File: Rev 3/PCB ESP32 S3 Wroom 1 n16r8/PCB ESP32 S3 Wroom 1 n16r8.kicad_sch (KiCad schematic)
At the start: 30 parts, among them J1 AudioJack3_SwitchT, M1 Haptic Feedback, Q1 BS170, SW1 Home, SW2 Back, SW3 Play/Pause, SW4 Power, SW5 Menu, SW6 Hold, SW7 BOOT_MODE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

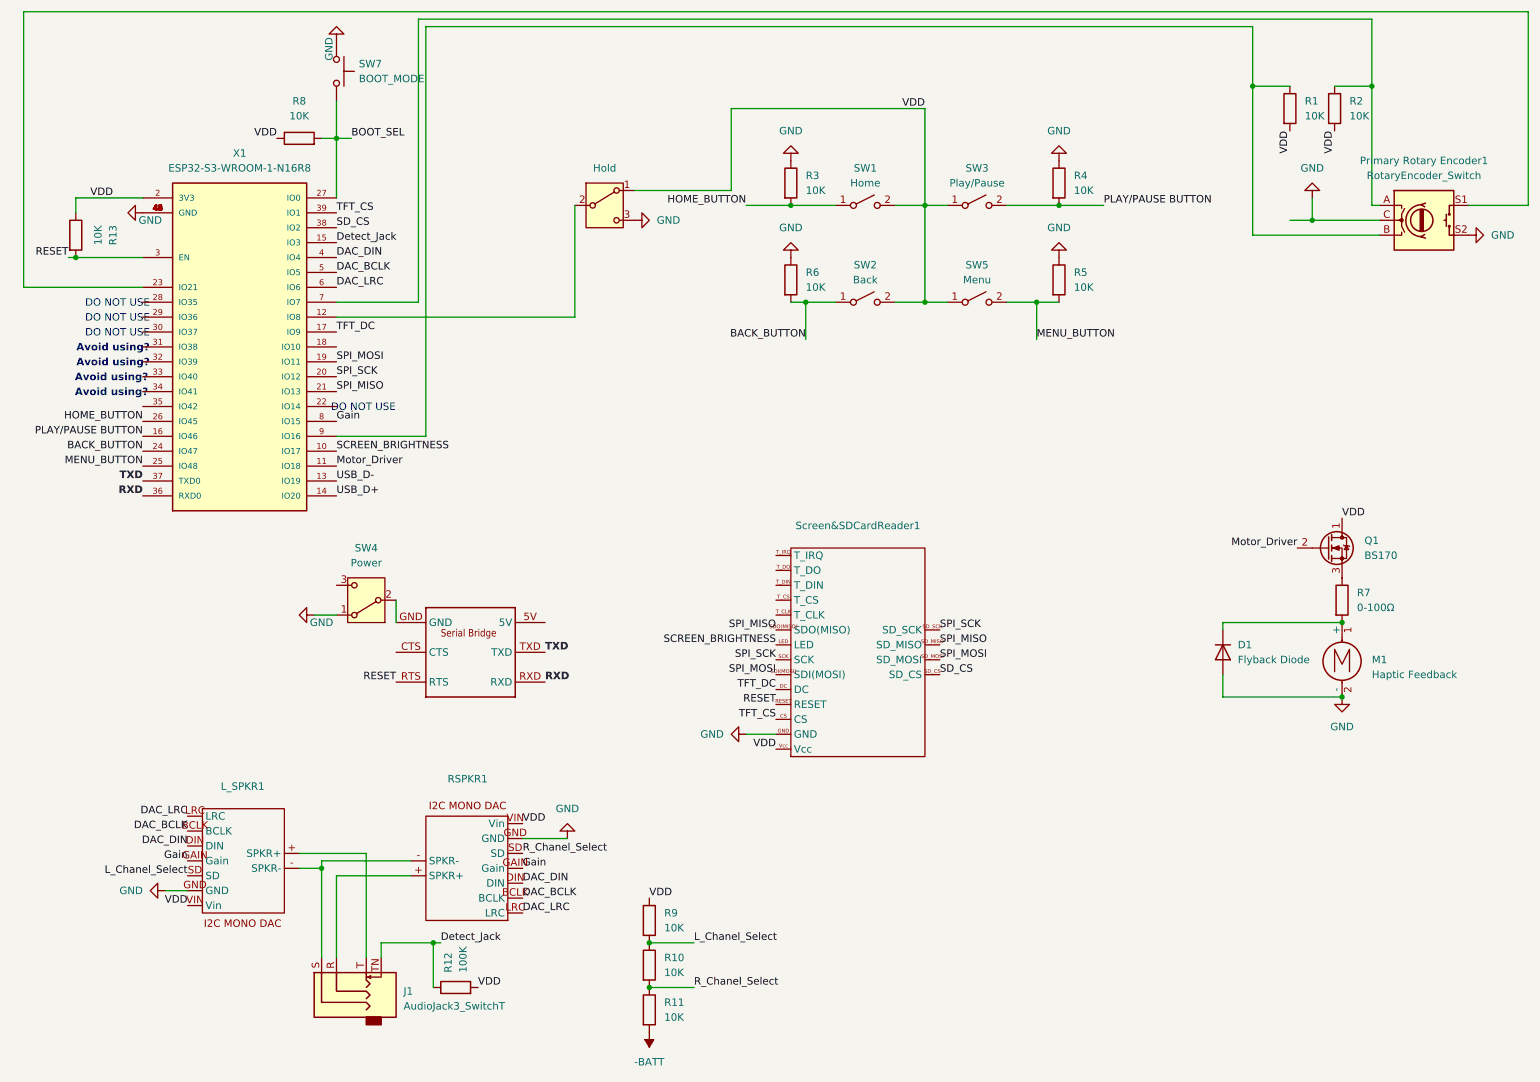
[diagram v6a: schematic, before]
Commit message: added 3v3 regulator
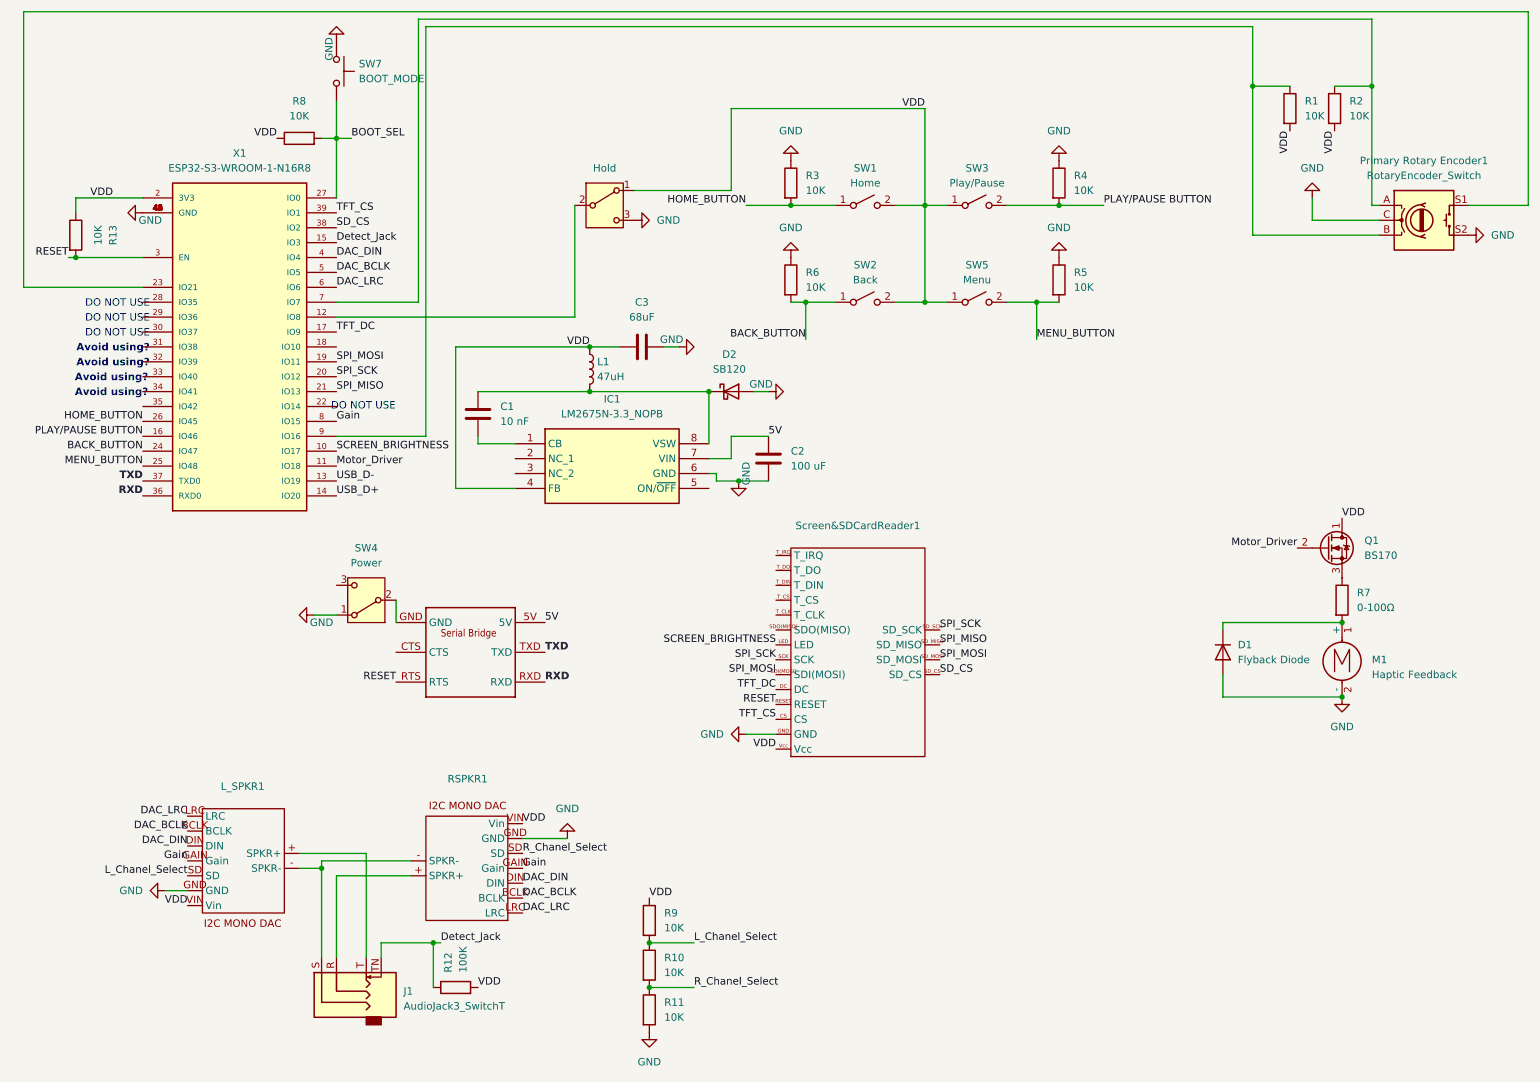
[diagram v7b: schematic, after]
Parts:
- added C1: 10 nF, Capacitor_SMD:C_2220_5750Metric, symbol Device:C
- added C2: 100 uF, Capacitor_SMD:C_2220_5750Metric, symbol Device:C
- added C3: 68uF, Capacitor_SMD:C_2220_5750Metric, symbol Device:C
- added D2: SB120, Diode_THT:D_DO-41_SOD81_P10.16mm_Horizontal, symbol Diode:SB120
- added IC1: LM2675N-3.3_NOPB, LM2675-3.3:DIP794W53P254L959H508Q8N, symbol LM2675N-3_3_NOPB:LM2675N-3.3_NOPB
- added L1: 47uH, Capacitor_SMD:C_0603_1608Metric, symbol Device:L
- 1: footprint (none) -> MP3_Player_Custom_Footprints:UART_FTDI
- SW7: footprint MP3_Player_Custom_Footprints:UART_FTDI -> Button_Switch_THT:SW_PUSH_6mm
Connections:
- net -BATT is gone; now on net GND: R11.2
- net GND: now also C2.1, C3.1, D2.2 (A), IC1.6 (GND)
- net SPI_MISO: no longer Screen&SDCardReader1.SDO(MISO)
- net VDD: now also C3.2, IC1.4 (FB), L1.1
- net 5V: now reaches 1.5V
- net 5V: now also C2.2, IC1.7 (VIN)
- new net: C1.1, D2.1 (K), IC1.8 (VSW), L1.2
- new net: C1.2, IC1.1 (CB)

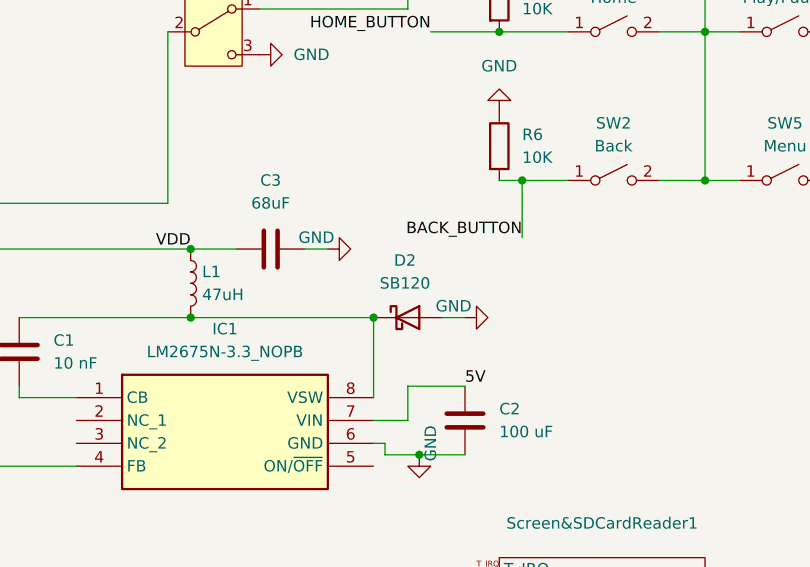
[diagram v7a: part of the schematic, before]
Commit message: updated d2 footprint
-1A, 40 V Schottky rectifier per datasheet
-package size determined from digikey
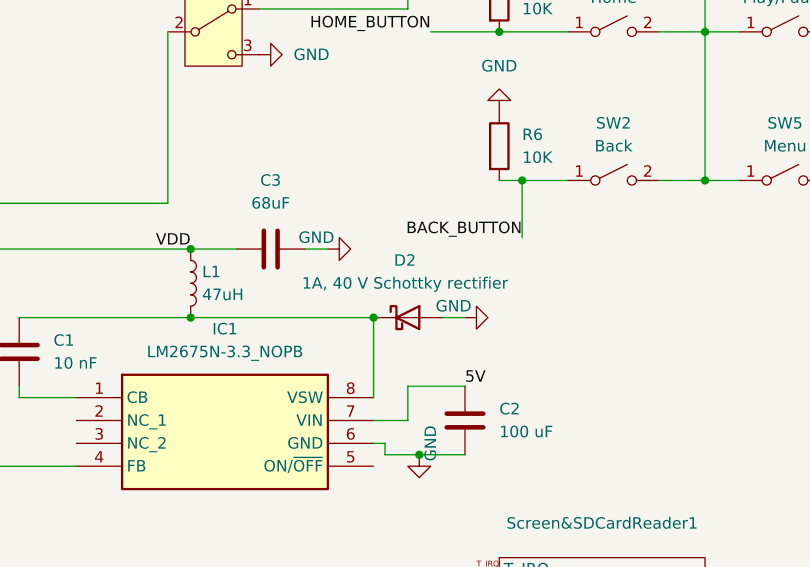
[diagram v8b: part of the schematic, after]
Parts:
- D2: value SB120 -> 1A, 40 V Schottky rectifier; footprint Diode_THT:D_DO-41_SOD81_P10.16mm_Horizontal -> Diode_SMD:D_SOD-323_HandSoldering
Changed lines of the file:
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@@
 			)
 		)
-		(property "Value" "SB120"
+		(property "Value" "1A, 40 V Schottky rectifier"
 			(at 139.3825 73.66 0)
 			(effects
@@
 			)
 		)
-		(property "Footprint" "Diode_THT:D_DO-41_SOD81_P10.16mm_Horizontal"
+		(property "Footprint" "Diode_SMD:D_SOD-323_HandSoldering"
 			(at 139.7 81.915 0)
 			(effects
